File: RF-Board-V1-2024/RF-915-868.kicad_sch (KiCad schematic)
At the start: 10 parts, among them J4 UART, J5 Conn_Coaxial, U5 MAX-M10S

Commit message: i think schematic is done for now
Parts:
- removed C12, C20: 100nF, symbol Device:C
- removed J4: UART, symbol Connector:Conn_01x02_Pin
- removed J5: Conn_Coaxial, footprints:TAOGLAS_EMPCB.SMAFSTJ.B.HT, symbol Connector:Conn_Coaxial
- removed RF2: VG2392S240X0M2, symbol ecocad_lib_symbols:Vollgo_2.4GHz
- removed TP1, TP2, TP3, TP4: TestPoint, symbol Connector:TestPoint
- removed U5: MAX-M10S, RF_GPS:ublox_MAX, symbol RF_GPS:MAX-M10S
- added C19, C21: 100nF, symbol Device:C
- added J2, J3: Conn_Coaxial, footprints:TAOGLAS_EMPCB.SMAFSTJ.B.HT, symbol Connector:Conn_Coaxial
- added RF3: DL-RFM69HC-915M, RF_Module:HOPERF_RFM9XW_THT, symbol RF_Module:RFM69HCW
- added RF4: RFM95W-868S2, symbol RF_Module:RFM95W-868S2
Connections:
- net +3.3V: now also C19.2, C21.2, RF3.13 (3.3V), RF4.13 (3.3V)
- net GND: now also C19.1, C21.1, J2.2 (Ext), J3.2 (Ext), RF3.1 (GND), RF3.10 (GND), RF3.8 (GND), RF4.1 (GND), RF4.10 (GND), RF4.8 (GND)
- new net 868.DIO0: RF4.14 (DIO0)
- new net 868.DIO1: RF4.15 (DIO1)
- new net 868.DIO2: RF4.16 (DIO2)
- new net 868.DIO3: RF4.11 (DIO3)
- new net 868.DIO4: RF4.12 (DIO4)
- new net 868.DIO5: RF4.7 (DIO5)
- new net 868.MISO: RF4.2 (MISO)
- new net 868.MOSI: RF4.3 (MOSI)
- new net 868.NSS: RF4.5 (NSS)
- new net 868.RST: RF4.6 (RESET)
- new net 868.SCK: RF4.4 (SCK)
- new net 915.DIO0: RF3.14 (DIO0)
- new net 915.DIO1: RF3.15 (DIO1)
- new net 915.DIO2: RF3.16 (DIO2)
- new net 915.DIO3: RF3.11 (DIO3)
- new net 915.DIO4: RF3.12 (DIO4)
- new net 915.DIO5: RF3.7 (DIO5)
- new net 915.MISO: RF3.2 (MISO)
- new net 915.MOSI: RF3.3 (MOSI)
- new net 915.NSS: RF3.5 (NSS)
- new net 915.RST: RF3.6 (RESET)
- new net 915.SCK: RF3.4 (SCK)
- new net ANT_868: J3.1 (In), RF4.9 (ANT)
- new net ANT_915: J2.1 (In), RF3.9 (ANT)
- no-connect marks 1 -> 0
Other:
- note added: "109990166 868MHz LoRa"
- note added: "DL-RFM69HC-915M 915MHz LoRa"
- note removed: "MAX-M10S GNSS"
- note removed: "active low"
- title: (none) -> RF 868MHz 915MHz

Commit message: sd card need to do gnss
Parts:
- added C14, C17: 100u, Capacitor_SMD:CP_Elec_6.3x5.9, symbol Device:C_Polarized
- added C15, C16: 10u, symbol Device:C
- added D6, D8: LED, LED_SMD:LED_0603_1608Metric, symbol Device:LED
- added R15, R17: 140R, Resistor_SMD:R_0603_1608Metric, symbol Device:R
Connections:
- net +3.3V: now also C14.1, C15.2, C16.2, C17.1
- net 868.NSS: now also D8.2 (A)
- net 915.NSS: now also D6.2 (A)
- net GND: now also C14.2, C15.1, C16.1, C17.2, R15.2, R17.2
- new net: D8.1 (K), R17.1
- new net: D6.1 (K), R15.1

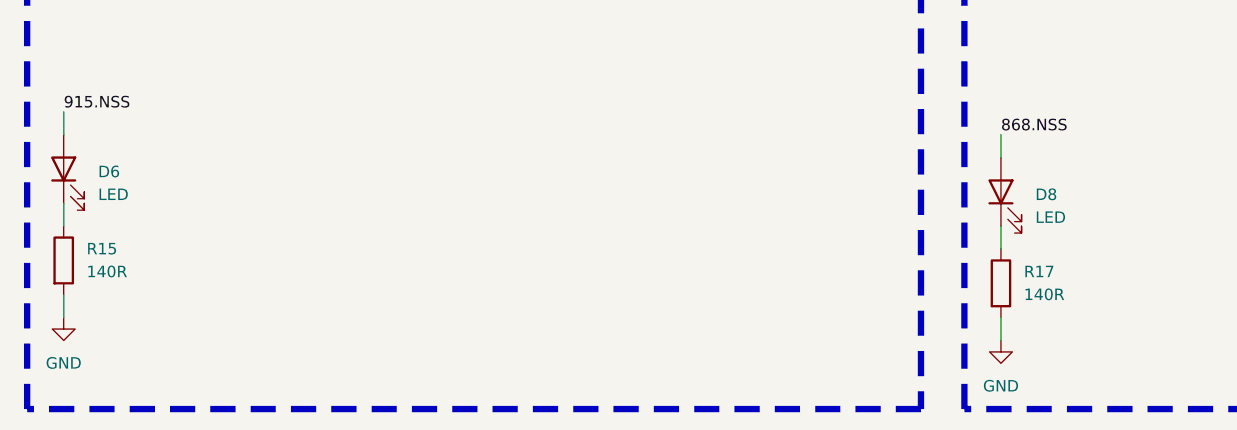
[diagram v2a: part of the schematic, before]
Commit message: changed the led resistors to 1k
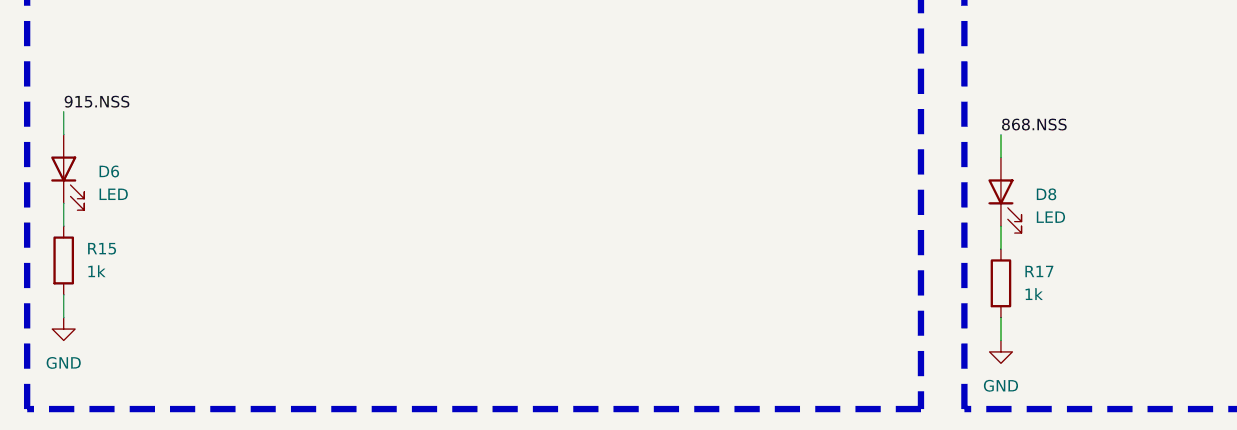
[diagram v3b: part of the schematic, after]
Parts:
- R15, R17: value 140R -> 1k
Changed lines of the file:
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@@
 			)
 		)
-		(property "Value" "140R"
+		(property "Value" "1k"
 			(at 125.73 129.5399 0)
 			(effects
@@
 			)
 		)
-		(property "Value" "140R"
+		(property "Value" "1k"
 			(at 21.59 126.9999 0)
 			(effects

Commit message: schematic done
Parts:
- removed D8: LED, LED_SMD:LED_0603_1608Metric, symbol Device:LED
- removed J2, J3: Conn_Coaxial, footprints:TAOGLAS_EMPCB.SMAFSTJ.B.HT, symbol Connector:Conn_Coaxial
- removed R17: 1k, Resistor_SMD:R_0603_1608Metric, symbol Device:R
- added D4: LED, LED_SMD:LED_0603_1608Metric, symbol Device:LED
- added J2, J3: RFPC-SMA29-F, ecocad_lib_footprints:GRADCONN_RFPC-SMA29-F, symbol ecocad_lib_symbols:RFPC-SMA29-F
- added R12: 600, Resistor_SMD:R_0603_1608Metric, symbol Device:R
- R15: value 1k -> 600
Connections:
- net 868.NSS: now also R12.1
- net 915.NSS: now also R15.1; no longer D6.2 (A)
- net ANT_868: now also J3.1
- net ANT_915: now also J2.1
- net GND: now also D6.1 (K), D4.1 (K), J2.G1, J2.G2, J2.G3, J2.G4, J3.G1, J3.G2, J3.G3, J3.G4; no longer R15.2
- new net: D4.2 (A), R12.2
- new net: D6.2 (A), R15.2

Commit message: basic layout done
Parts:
- added C38, C45: 100n, Capacitor_SMD:C_0805_2012Metric, symbol Device:C
- added R28: 10k, Resistor_SMD:R_0805_2012Metric, symbol Device:R
- added R29: 0, Resistor_SMD:R_0805_2012Metric, symbol Device:R
- added SW3, SW6: SW_SPST, Button_Switch_SMD:SW_DIP_SPSTx01_Slide_6.7x4.1mm_W6.73mm_P2.54mm_LowProfile_JPin, symbol Switch:SW_SPST
- C15, C16: footprint (none) -> Capacitor_SMD:C_0805_2012Metric
- C19, C21: value 100nF -> 100n; footprint (none) -> Capacitor_SMD:C_0805_2012Metric
- D4, D6: footprint LED_SMD:LED_0603_1608Metric -> LED_SMD:LED_0805_2012Metric
- R12, R15: footprint Resistor_SMD:R_0603_1608Metric -> Resistor_SMD:R_0805_2012Metric
- RF3: footprint RF_Module:HOPERF_RFM9XW_THT -> RF_Module:HOPERF_RFM9XW_SMD; LCSC # (none) -> C2844478; LSCS # C2844478 -> (none)
- RF4: footprint (none) -> RF_Module:HOPERF_RFM9XW_SMD; DK # (none) -> 1597-1488-ND; DK# 1597-1488-ND -> (none)
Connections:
- net +3.3V: now also R28.1, R29.1
- net 868.RST: now also C45.1, R29.2, SW6.2 (B)
- net 915.RST: now also C38.1, R28.2, SW3.2 (B)
- net GND: now also C38.2, C45.2, SW3.1 (A), SW6.1 (A)

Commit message: cyhanged buttons
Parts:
- SW3, SW6: footprint Button_Switch_SMD:SW_DIP_SPSTx01_Slide_6.7x4.1mm_W6.73mm_P2.54mm_LowProfile_JPin -> Button_Switch_THT:SW_PUSH_6mm
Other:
- company: (none) -> University Of Alberta EcoCar Team
- title: RF 868MHz 915MHz -> UltraCom Telemetry
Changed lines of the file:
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@@
 	(paper "A4")
 	(title_block
-		(title "RF 868MHz 915MHz")
+		(title "UltraCom Telemetry")
+		(rev "Series. 1")
+		(company "University Of Alberta EcoCar Team")
 	)
 	(junction
@@
 			)
 		)
-		(property "Footprint" "Button_Switch_SMD:SW_DIP_SPSTx01_Slide_6.7x4.1mm_W6.73mm_P2.54mm_LowProfile_JPin"
+		(property "Footprint" "Button_Switch_THT:SW_PUSH_6mm"
 			(at 95.25 121.92 0)
 			(effects
@@
 			)
 		)
-		(property "Footprint" "Button_Switch_SMD:SW_DIP_SPSTx01_Slide_6.7x4.1mm_W6.73mm_P2.54mm_LowProfile_JPin"
+		(property "Footprint" "Button_Switch_THT:SW_PUSH_6mm"
 			(at 201.93 123.19 0)
 			(effects

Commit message: whatever
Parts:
- R28: value 10k -> 0R; now not fitted
- R29: value 0 -> 0R
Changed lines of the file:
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@@
 		(in_bom yes)
 		(on_board yes)
-		(dnp no)
+		(dnp yes)
 		(fields_autoplaced yes)
 		(property "Reference" "R28"
@@
 			)
 		)
-		(property "Value" "10k"
+		(property "Value" "0R"
 			(at 104.14 116.8399 0)
 			(effects
@@
 			)
 		)
-		(property "Value" "0"
+		(property "Value" "0R"
 			(at 210.82 118.1099 0)
 			(effects

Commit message: AA
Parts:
- D4, D6: footprint LED_SMD:LED_0805_2012Metric -> LED_SMD:LED_0603_1608Metric
- R12, R15, R28, R29: footprint Resistor_SMD:R_0805_2012Metric -> Resistor_SMD:R_0603_1608Metric
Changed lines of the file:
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@@
 			)
 		)
-		(property "Footprint" "Resistor_SMD:R_0805_2012Metric"
+		(property "Footprint" "Resistor_SMD:R_0603_1608Metric"
 			(at 99.822 115.57 90)
 			(effects
@@
 			)
 		)
-		(property "Footprint" "LED_SMD:LED_0805_2012Metric"
+		(property "Footprint" "LED_SMD:LED_0603_1608Metric"
 			(at 123.19 128.27 0)
 			(effects
@@
 			)
 		)
-		(property "Footprint" "Resistor_SMD:R_0805_2012Metric"
+		(property "Footprint" "Resistor_SMD:R_0603_1608Metric"
 			(at 121.412 118.11 90)
 			(effects
@@
 			)
 		)
-		(property "Footprint" "LED_SMD:LED_0805_2012Metric"
+		(property "Footprint" "LED_SMD:LED_0603_1608Metric"
 			(at 19.05 127 0)
 			(effects
@@
 			)
 		)
-		(property "Footprint" "Resistor_SMD:R_0805_2012Metric"
+		(property "Footprint" "Resistor_SMD:R_0603_1608Metric"
 			(at 17.272 116.84 90)
 			(effects
@@
 			)
 		)
-		(property "Footprint" "Resistor_SMD:R_0805_2012Metric"
+		(property "Footprint" "Resistor_SMD:R_0603_1608Metric"
 			(at 206.502 116.84 90)
 			(effects
